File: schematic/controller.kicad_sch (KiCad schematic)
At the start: 38 parts, among them J5 DB9_Male, J6 DB9_Male, Q4 2N3904, Q5 2N3904, U18 74LS541, U19 74LS541, U24 74LS00

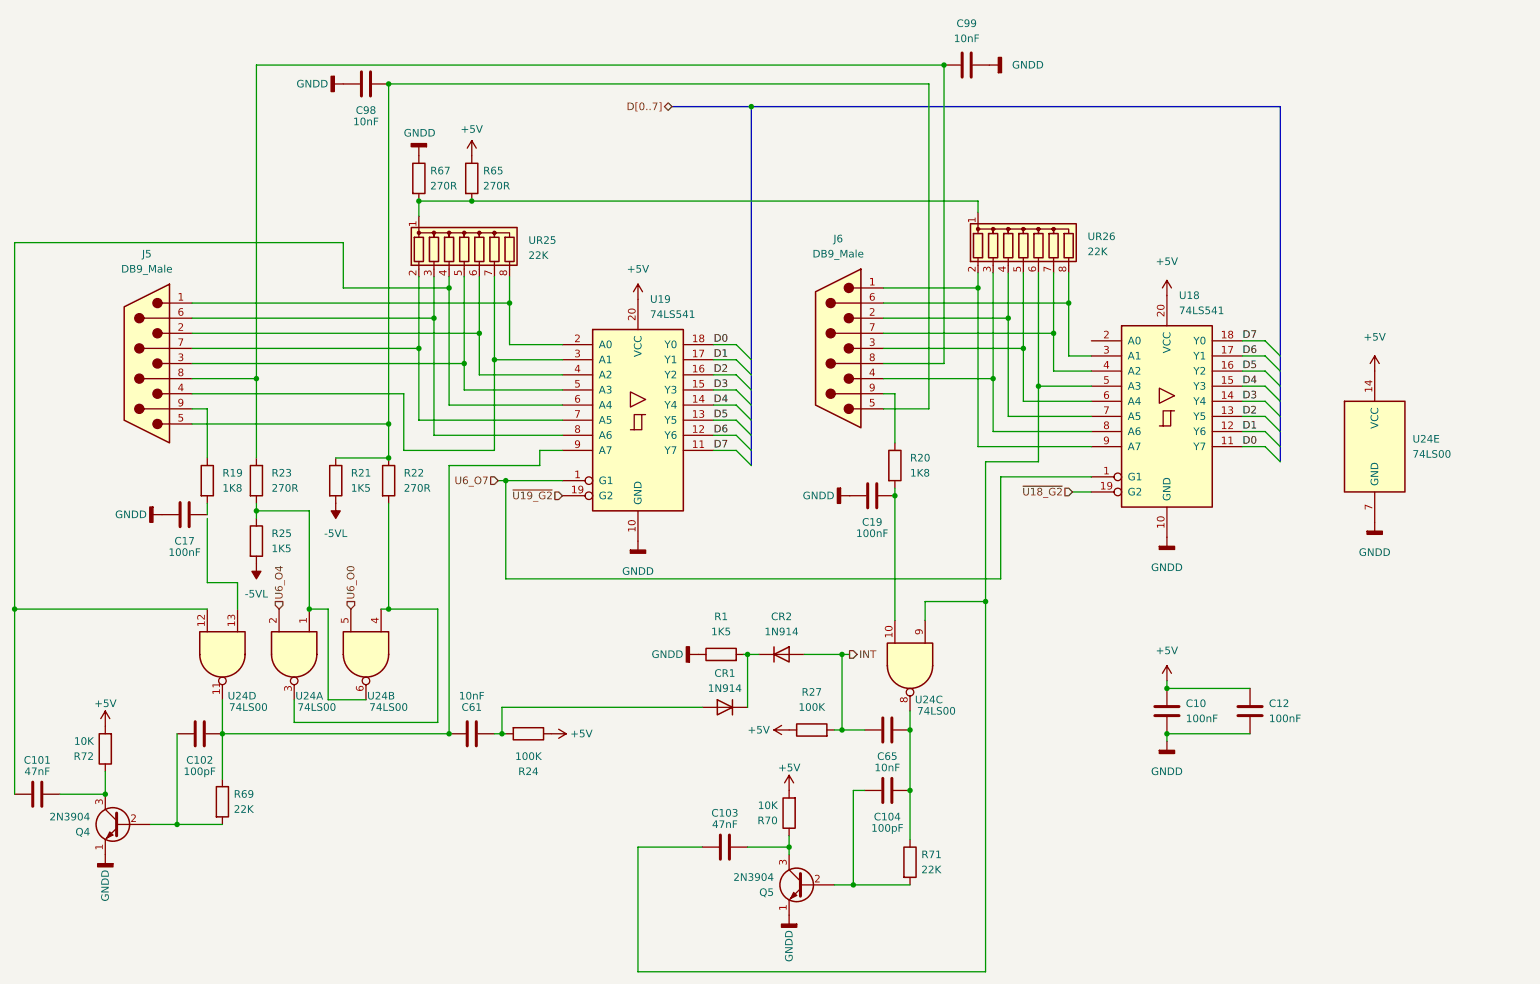
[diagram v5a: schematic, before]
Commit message: altered and did some cleanup of the way the wires were run. Finished expansion port routes to rf modulator. Added ext_psu for future external power supply design (will be an off the shelf psu block).
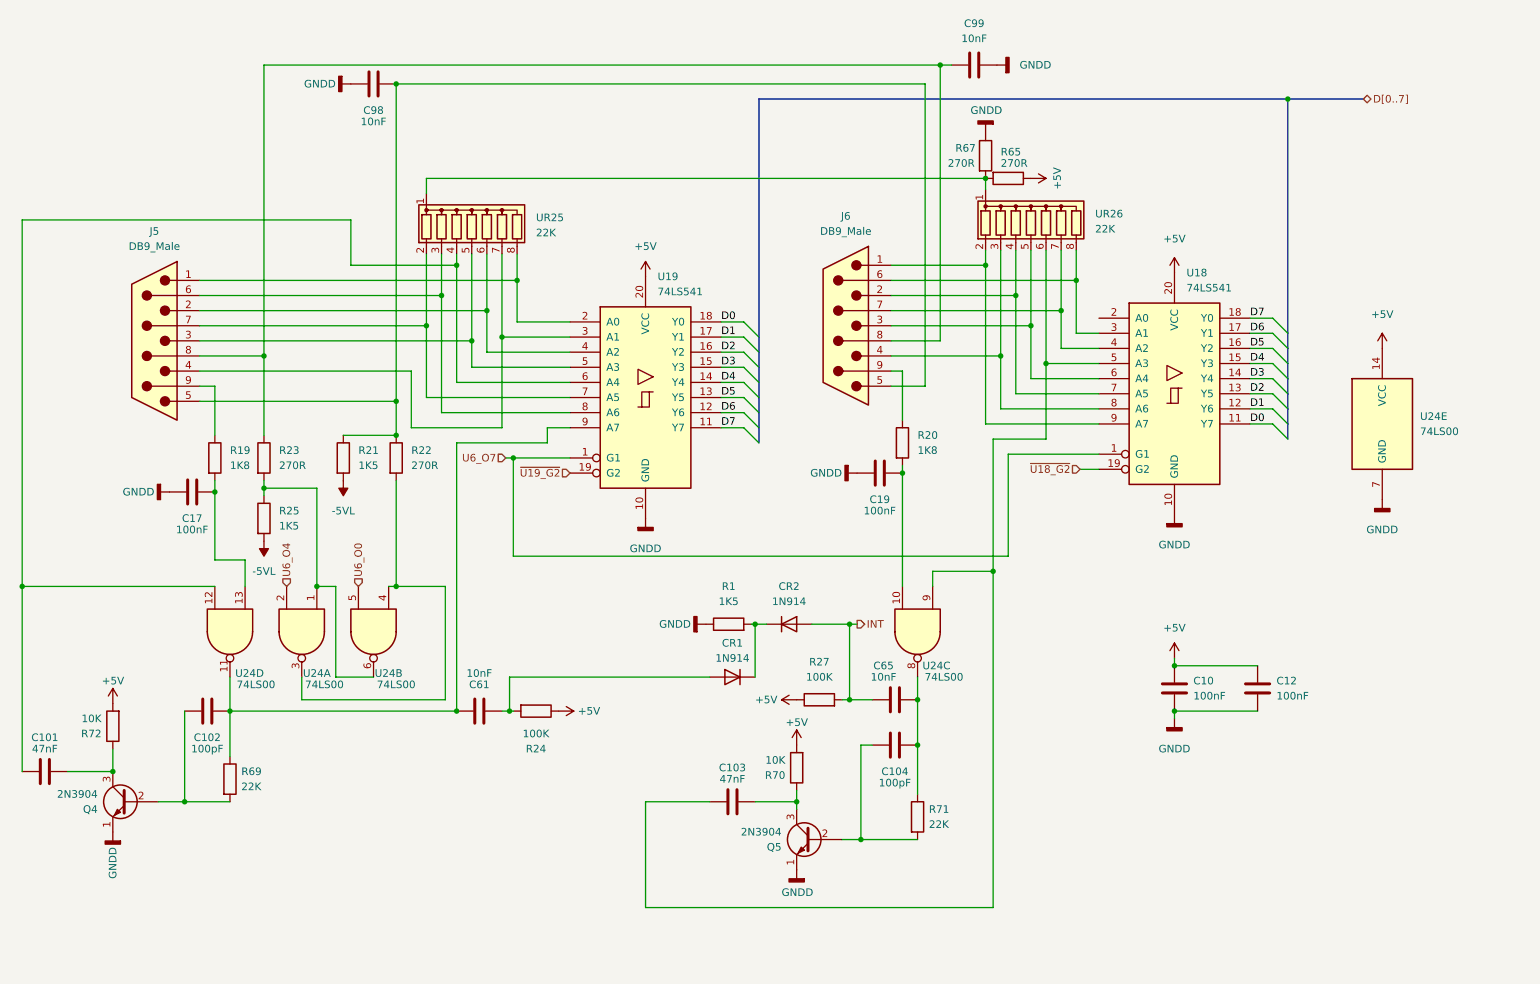
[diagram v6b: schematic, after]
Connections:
- net at U24.13: now also C17.2, R19.2
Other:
- moved on the sheet: C10, C101, C102, C103, C104, C12, C17, C19, C61, C65, C98, C99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

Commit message: cleanup on the controller schematic. Checked against wiki.console5.com/wiki/Colecovision. Found a mistake with INT line thanks to the wiki. R21/R22 is reversed between the schematics. Aka R21 is placed on the output of 3. Which actually makes sense, but isn't the way its done on my REV F. R25/R23 match the wiki and that has R25 the pull down on the output pin 6 of the nand. Looks like R21 is a board mistake, but I'll keep it in since its correct for documentation purposes.
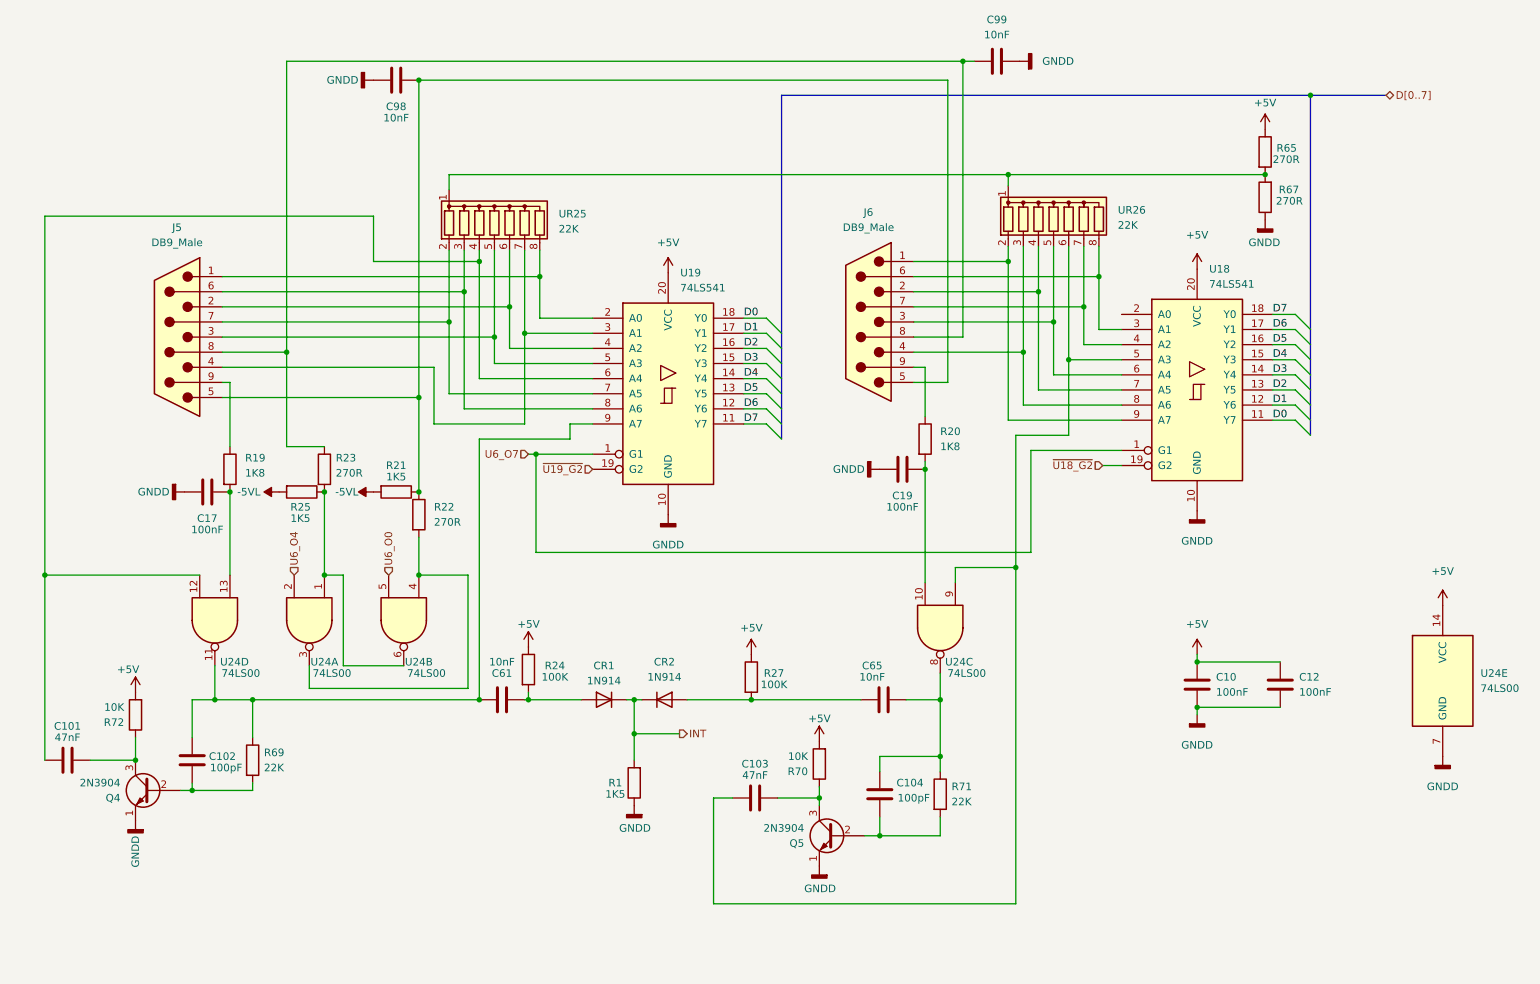
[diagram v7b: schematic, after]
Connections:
- net INT: now also CR1.1 (K), CR2.1 (K), R1.2; no longer C65.1, CR2.2 (A), R27.2
- new net: C65.1, CR2.2 (A), R27.2
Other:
- moved on the sheet: C10, C101, C102, C103, C104, C12, C17, C19, C61, C65, C98, C99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

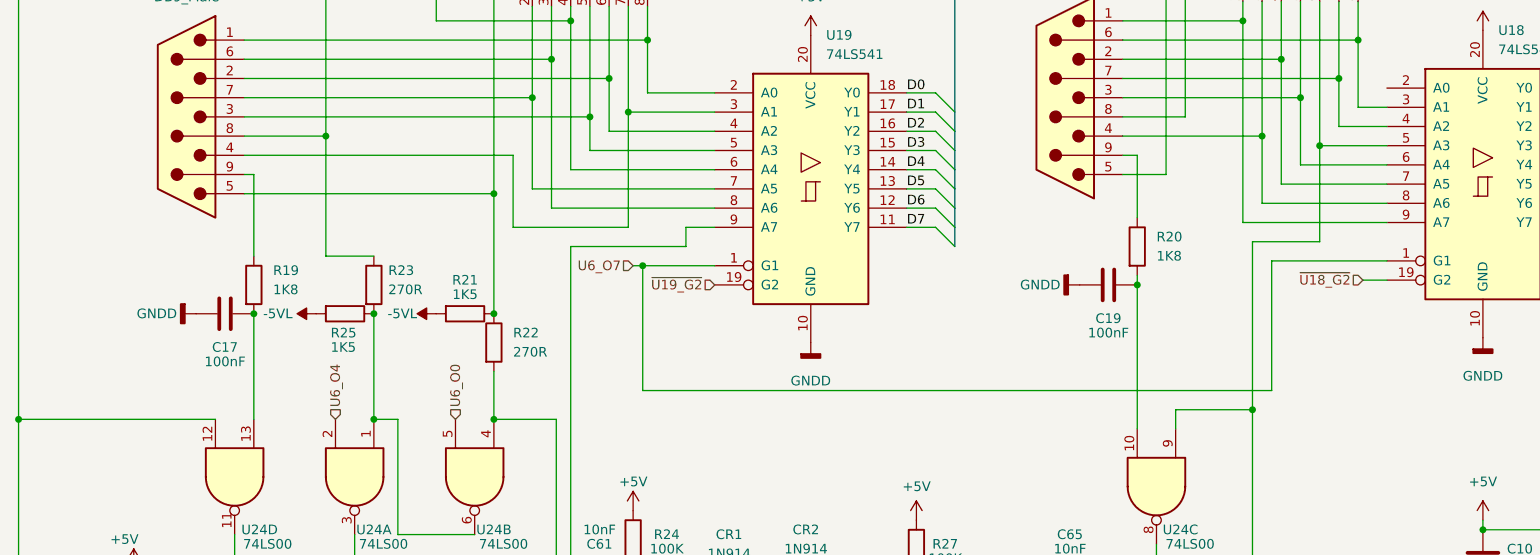
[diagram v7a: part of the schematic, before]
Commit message: all lines renamed, based most of the names from the coleco adam schematic. CS cart lines are my own, and the rest are from the wiki schematic for the controller... those will need to be checked.
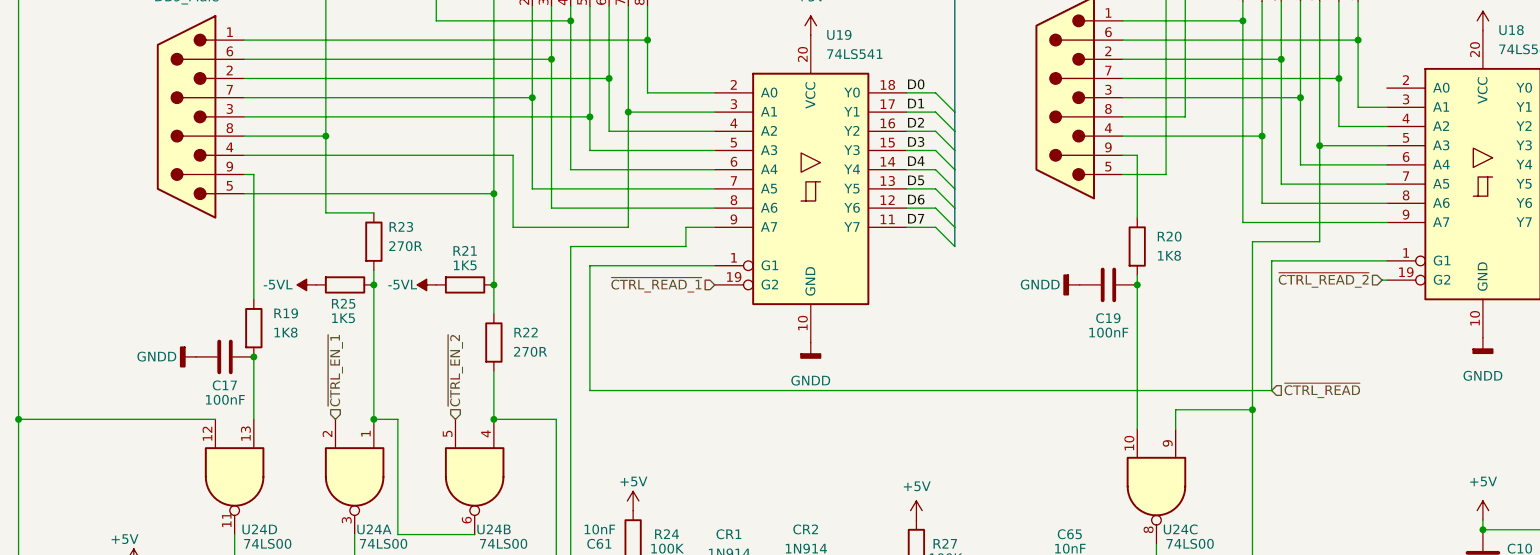
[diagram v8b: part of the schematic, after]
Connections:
- net U6_O0 renamed ~{CTRL_EN_2}
- net U6_O4 renamed ~{CTRL_EN_1}
- net U6_O7 renamed ~{CTRL_READ}
- net ~{U18_G2} renamed ~{CTRL_READ_2}
- net ~{U19_G2} renamed ~{CTRL_READ_1}
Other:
- moved on the sheet: C17, R19, R21, R23, R25
